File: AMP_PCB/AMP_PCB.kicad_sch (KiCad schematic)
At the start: 18 parts, among them J1 Conn_Coaxial, J2 Conn_Coaxial, J5 Conn_01x02_Pin

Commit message: updated schematic with OP
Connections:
- net GND: now also Vgate2.2; no longer Vgate2.1
- net Vgate2: now also Vgate2.1; no longer Vgate2.2
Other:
- moved on the sheet: Vgate2
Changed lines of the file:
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@@
 			)
 		)
-		(property "Sim.Library" "C:\\Users\\User\\Documents\\GitHub\\EE_348_StudentFiles_FinalProj\\JFE150\\jfe150.lib"
+		(property "Sim.Library" "/Users/phoebemeister/Desktop/EE_348_Final_Project_Main/FinalDesignProject348/JFE150/jfe150.lib"
 			(at 200.66 69.85 0)
 			(effects
@@
 			)
 		)
-		(property "Sim.Pins" "5=D 3=G 4=S 1=VCH 2=VCL"
+		(property "Sim.Pins" "1=VCH 2=VCL 3=G 4=S 5=D"
 			(at 200.66 69.85 0)
 			(effects
@@
 	(symbol
 		(lib_id "Simulation_SPICE:VSIN")
-		(at 248.92 69.85 270)
+		(at 248.92 69.85 90)
 		(unit 1)
 		(exclude_from_sim no)
@@
 		(dnp no)
 		(property "Reference" "Vgate2"
-			(at 243.586 67.818 90)
+			(at 254.254 71.882 90)
 			(effects
 				(font
@@
 		)
 		(property "Value" "VSIN"
-			(at 243.586 65.278 90)
+			(at 254.254 74.422 90)
 			(effects
 				(font
@@
 			)
 		)
-		(property "Sim.Params" "dc=0.1 ampl=0.1 f=1k ac=1"
-			(at 261.874 62.23 90)
+		(property "Sim.Params" "dc=0.1 ampl=-0.1 f=1k ac=-1"
+			(at 235.458 82.804 90)
 			(effects
 				(font
@@
 			)
 		)
-		(property "Sim.Library" "C:\\Users\\User\\Documents\\GitHub\\EE_348_StudentFiles_FinalProj\\JFE150\\jfe150.lib"
+		(property "Sim.Library" "/Users/phoebemeister/Desktop/EE_348_Final_Project_Main/FinalDesignProject348/JFE150/jfe150.lib"
 			(at 168.91 69.85 0)
 			(effects
@@
 			)
 		)
-		(property "Sim.Pins" "5=D 3=G 4=S 1=VCH 2=VCL"
+		(property "Sim.Pins" "1=VCH 2=VCL 3=G 4=S 5=D"
 			(at 168.91 69.85 0)
 			(effects

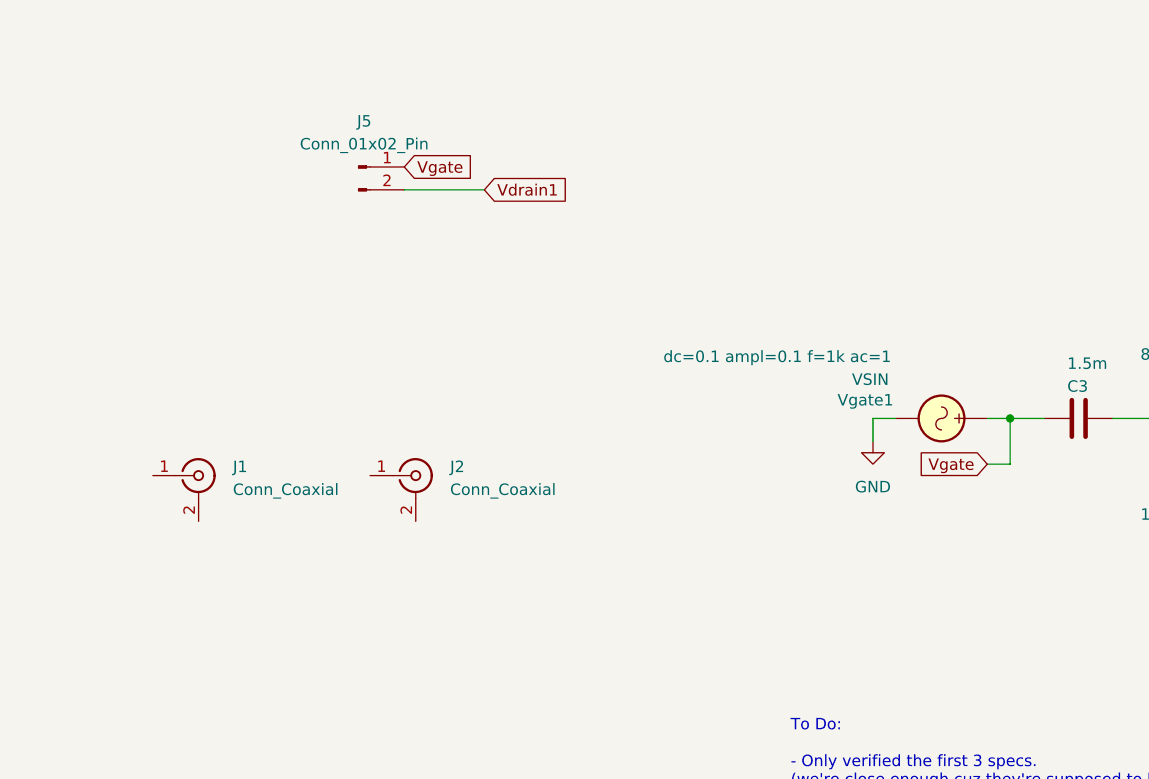
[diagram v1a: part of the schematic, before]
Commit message: Little changes to AMP schematic
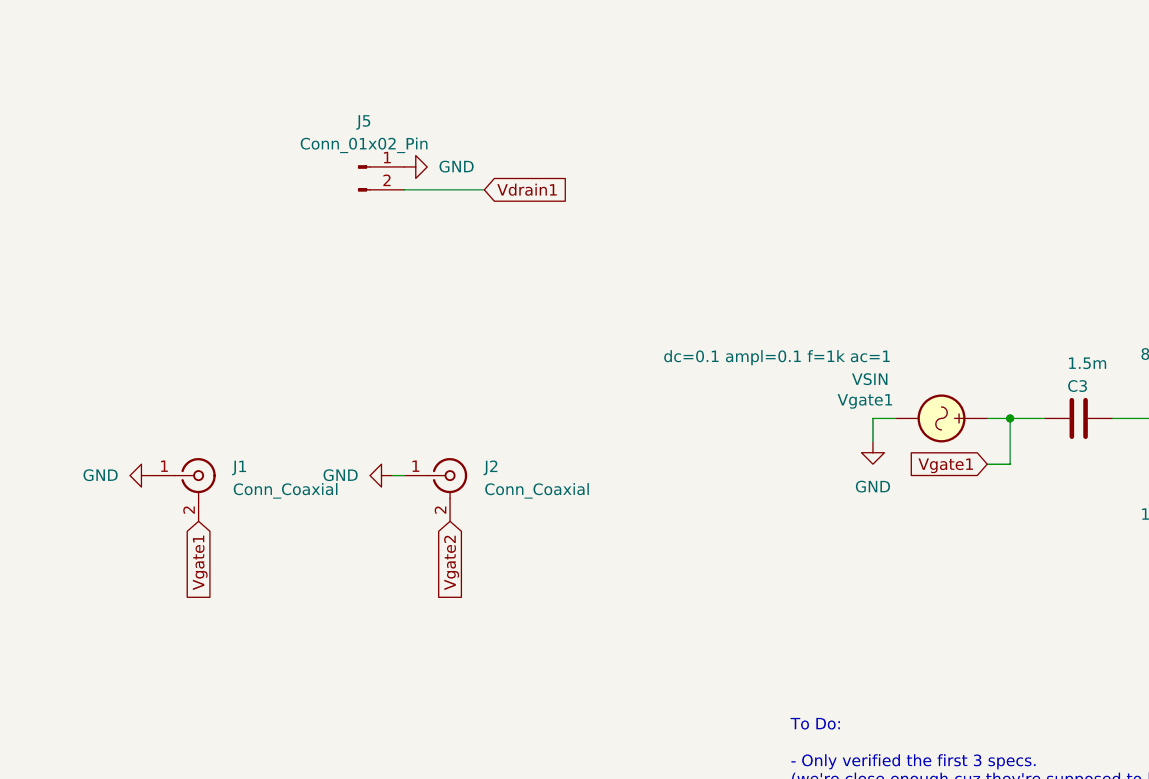
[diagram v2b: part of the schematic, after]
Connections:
- net GND: now also J1.1 (In), J2.1 (In), J5.1 (Pin_1)
- net Vgate2: now also J2.2 (Ext)
- net Vgate1: now reaches J1.2 (Ext)
- net Vgate1: now also C3.2, Vgate1.1
- removed net Vgate: C3.2, J5.1 (Pin_1), Vgate1.1
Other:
- moved on the sheet: J2

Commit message: updated footprint ver
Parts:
- removed Vgate1, Vgate2: VSIN, symbol Simulation_SPICE:VSIN
- added J3, J4: Conn_Coaxial, Connector_Coaxial:SMA_Samtec_SMA-J-P-H-ST-EM1_EdgeMount, symbol Connector:Conn_Coaxial
- added R2: 200, Resistor_SMD:R_1206_3216Metric, symbol Device:R_Small_US
- added R3: 5, Resistor_SMD:R_1206_3216Metric, symbol Device:R_Small_US
- added V1: Vgate1, symbol Simulation_SPICE:VSIN
- added V2: Vgate2, symbol Simulation_SPICE:VSIN
- C1, C2: footprint (none) -> Capacitor_SMD:C_1206_3216Metric
- C3, C4: value 1.5m -> 100u; footprint (none) -> Capacitor_SMD:C_1206_3216Metric
- R1: value 205 -> 200; footprint (none) -> Resistor_SMD:R_1206_3216Metric
- R4: renamed from R2; value 205 -> 5; footprint (none) -> Resistor_SMD:R_1206_3216Metric
- R5: renamed from R3; value 80 -> 800; footprint (none) -> Resistor_SMD:R_1206_3216Metric
- R6: renamed from R5; value 80 -> 800; footprint (none) -> Resistor_SMD:R_1206_3216Metric
- R7: renamed from R4; value 1 -> 10; footprint (none) -> Resistor_SMD:R_1206_3216Metric
- R8: renamed from R6; value 1 -> 10; footprint (none) -> Resistor_SMD:R_1206_3216Metric
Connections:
- net GND: now also J3.1 (In), J4.1 (In), V1.2, V2.2
- net Vgate1: now also V1.1
- net Vgate2: now also V2.1
- net Vout2: now also J4.2 (Ext)
- net Vdrain1 renamed Vdd
- net Vdd: now also R2.1; no longer R4.1
- net Vout renamed Vout1
- net Vout1: now also J3.2 (Ext), R3.2; no longer R1.2
- new net: R1.2, R3.1
- new net: R2.2, R4.1
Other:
- moved on the sheet: J1, J2, R1, R4

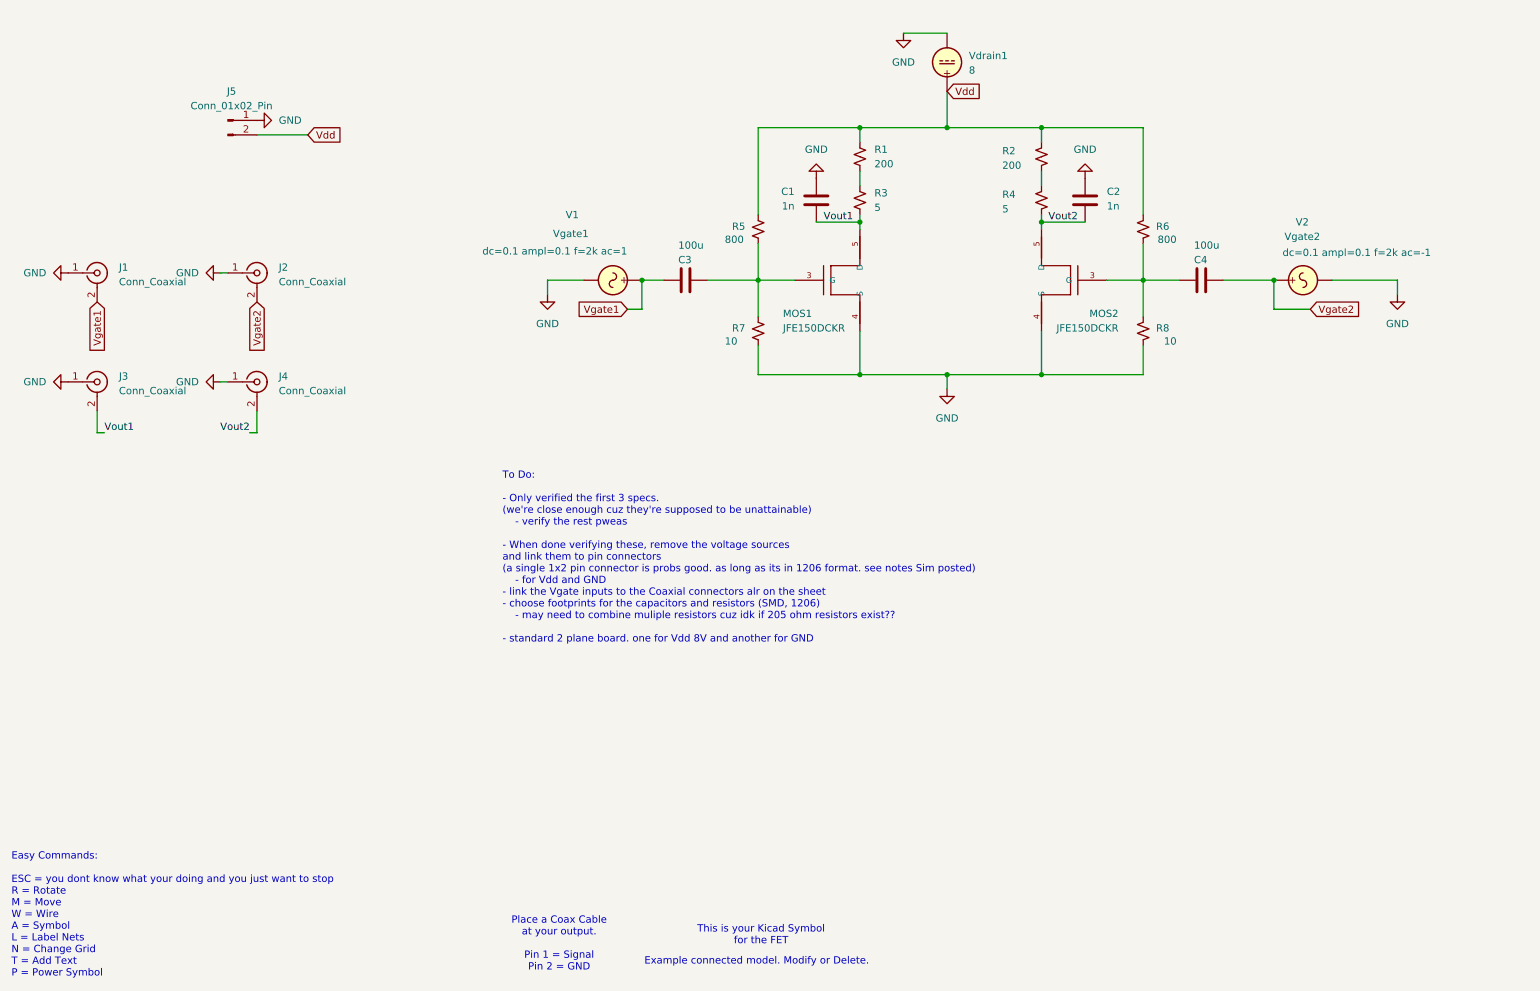
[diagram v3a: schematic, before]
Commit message: updated design + footprints
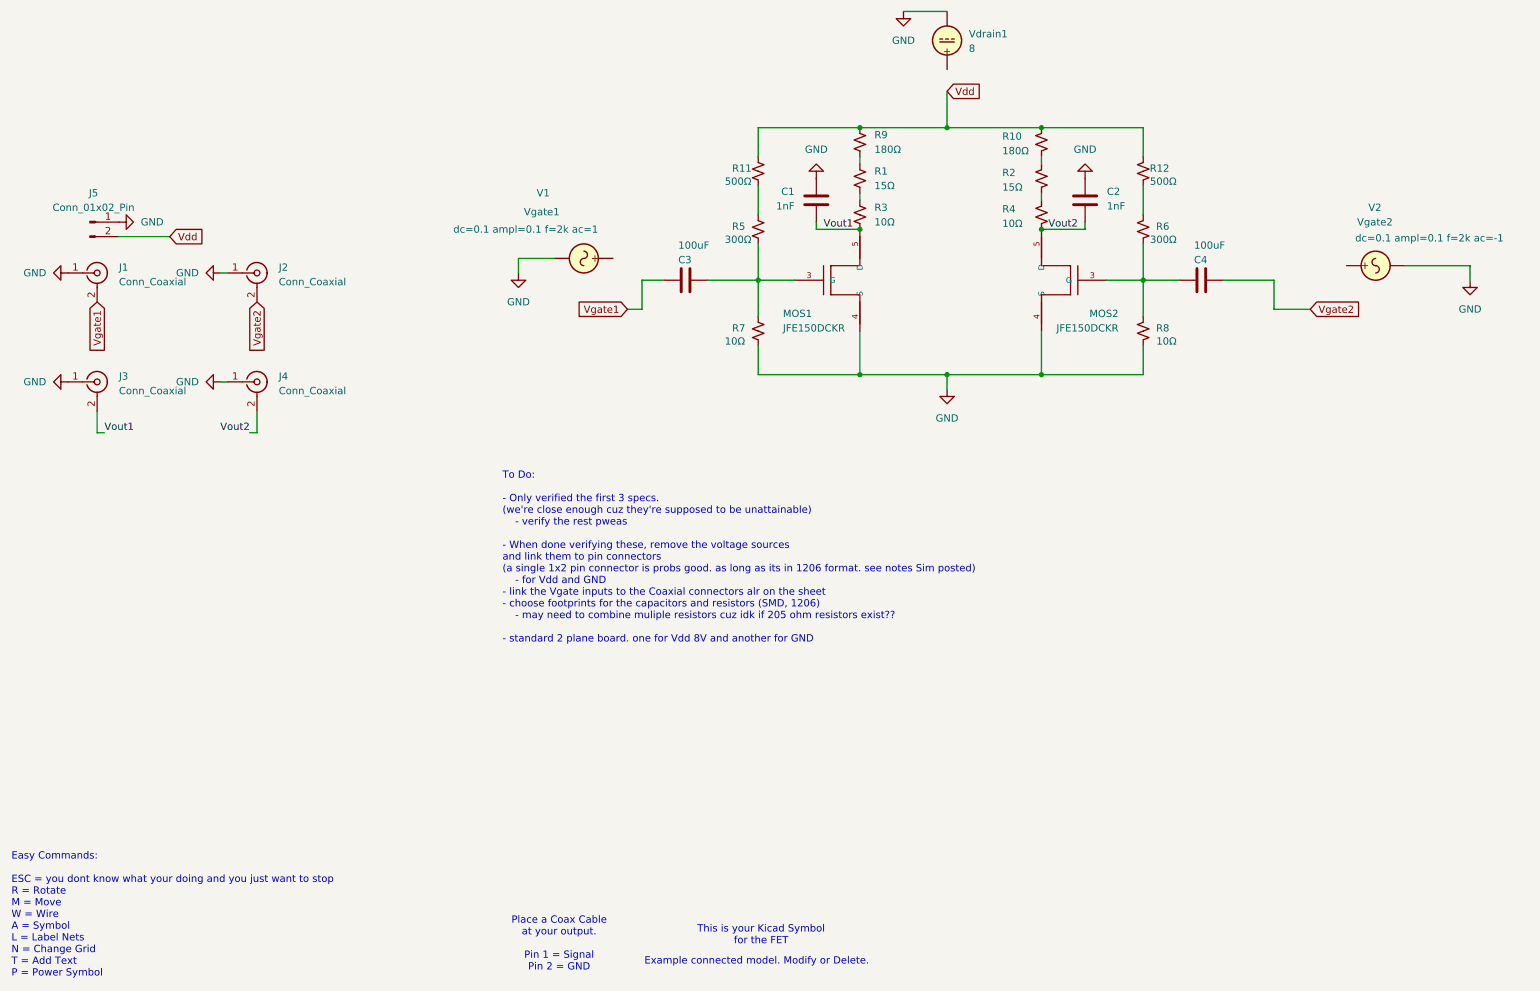
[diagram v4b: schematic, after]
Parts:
- added R10, R9: 180Ω, Resistor_SMD:R_1206_3216Metric, symbol Device:R_Small_US
- added R11, R12: 500Ω, Resistor_SMD:R_1206_3216Metric, symbol Device:R_Small_US
- C1, C2: value 1n -> 1nF
- C3, C4: value 100u -> 100uF
- R1, R2: value 200 -> 15Ω
- R3, R4: value 5 -> 10Ω
- R5, R6: value 800 -> 300Ω
- R7, R8: value 10 -> 10Ω
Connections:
- net Vdd: now also R10.1, R11.1, R12.1, R9.1; no longer R1.1, R2.1, R5.1, R6.1, Vdrain1.1
- net Vgate1: no longer V1.1
- net Vgate2: no longer V2.1
- new net: R11.2, R5.1
- new net: R1.1, R9.2
- new net: R10.2, R2.1
- new net: R12.2, R6.1
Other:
- moved on the sheet: J5, R1, R2, R3, R4, V1, V2, Vdrain1
